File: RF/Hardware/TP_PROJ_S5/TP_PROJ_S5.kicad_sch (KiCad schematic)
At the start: 28 parts, among them J1 Connecteur STLINK V3, J2 DIN-5, J3 Batterie, SW1 Reset Btn, U1 STM32WB55CEUx, U2 BU33SD5WG-TR, Y1 32k, Y2 32 MHZ

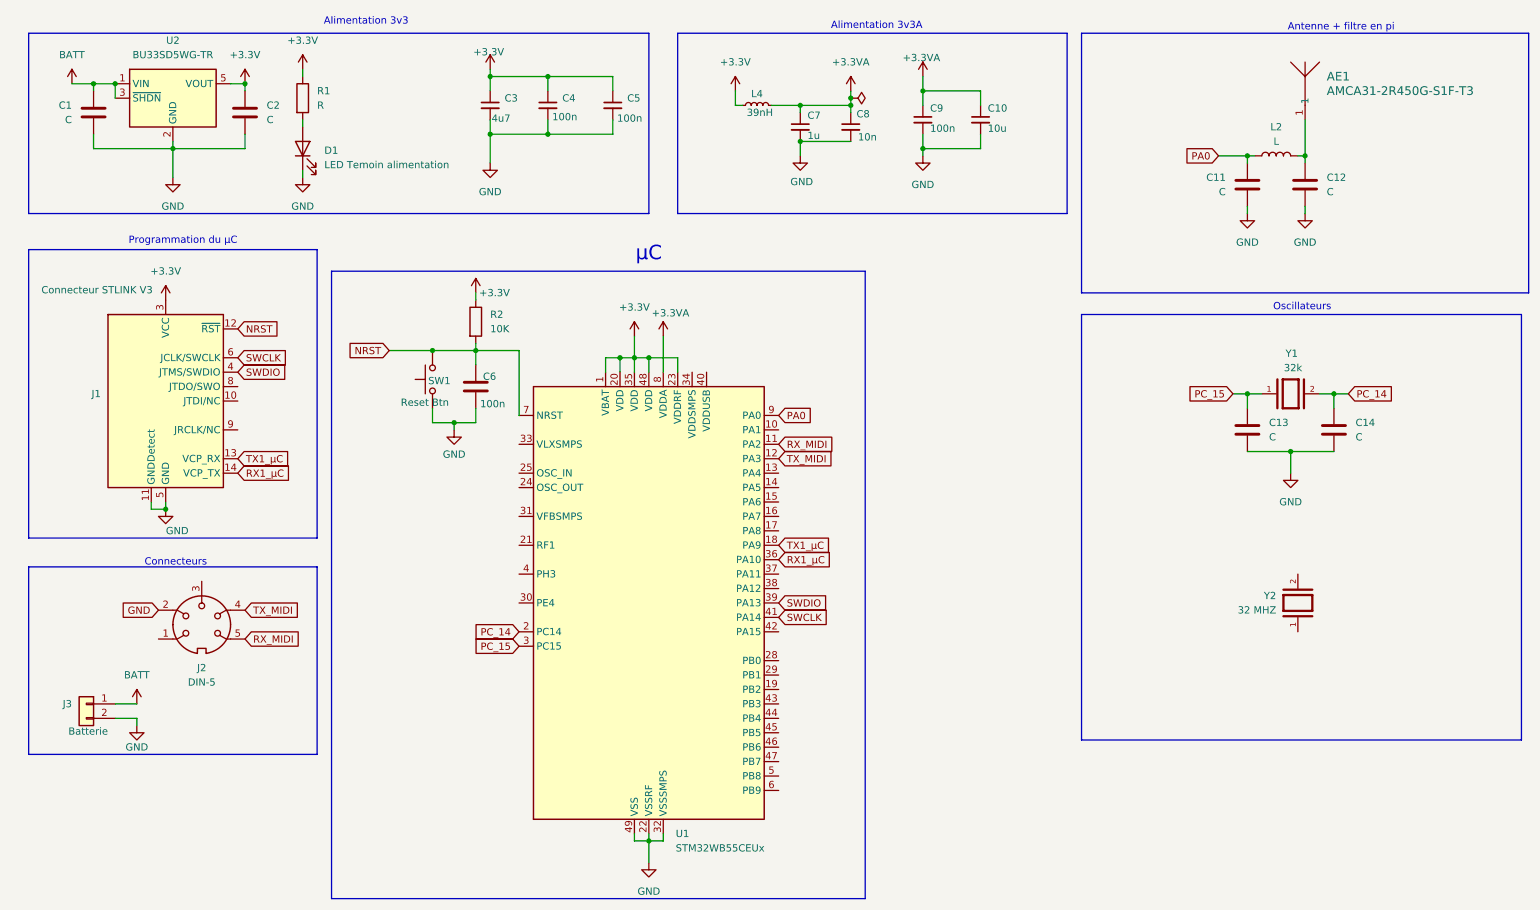
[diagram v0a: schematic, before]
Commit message: Schéma à priori fini, à revoir avec le prof
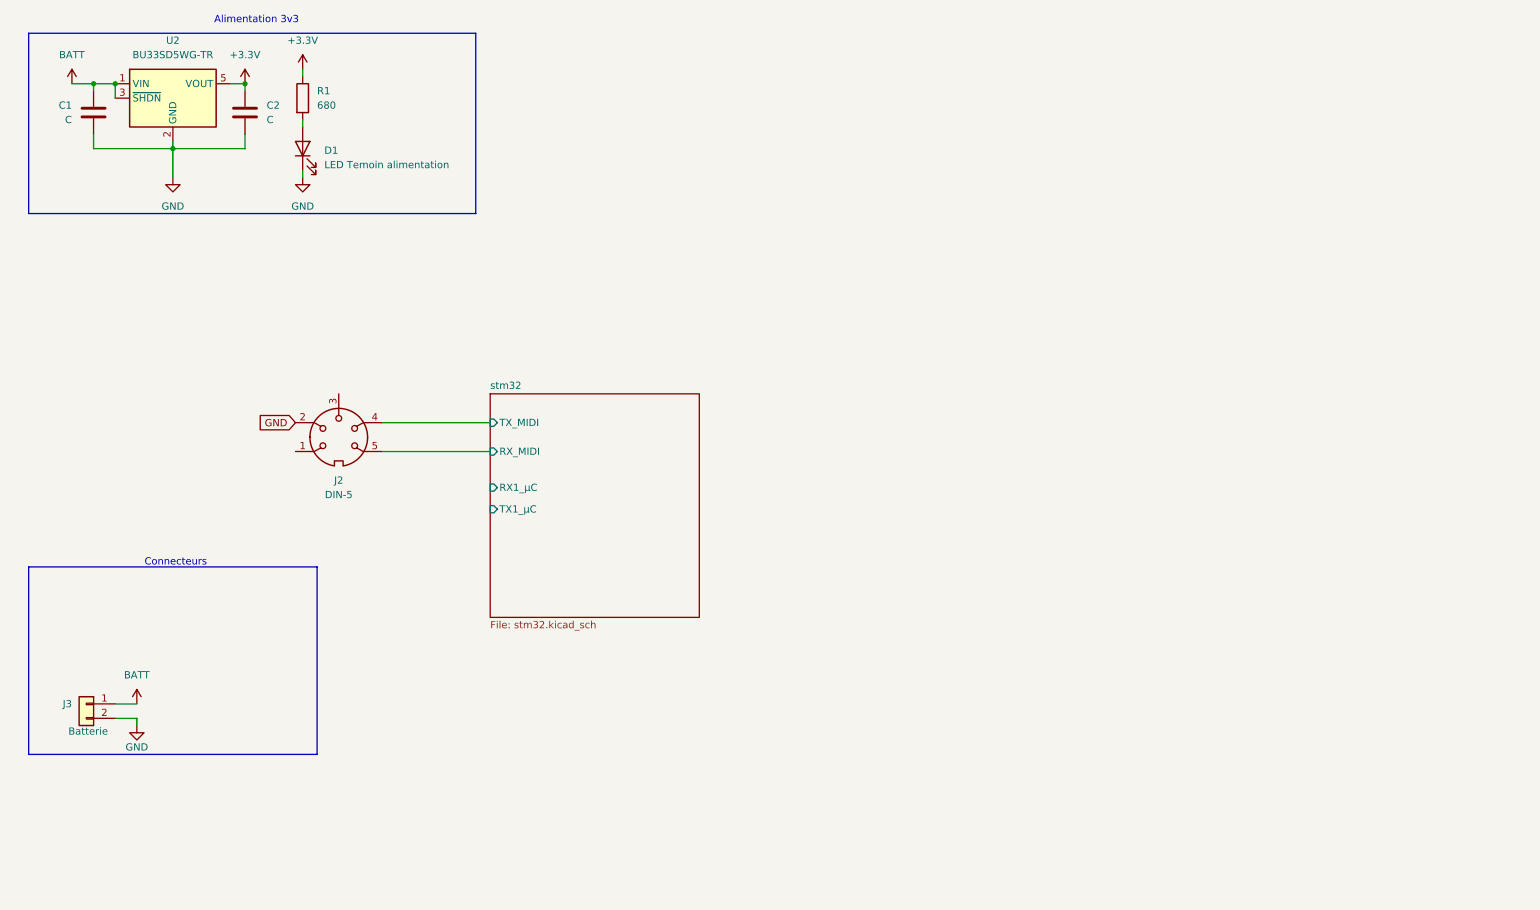
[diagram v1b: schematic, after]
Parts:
- removed AE1: AMCA31-2R450G-S1F-T3, ANT_AMCA31-2R450G-S1F-T3_ABR, symbol 2025-03-03_13-43-06:AMCA31-2R450G-S1F-T3
- removed C10: 10u, Capacitor_SMD:C_0603_1608Metric_Pad1.08x0.95mm_HandSolder, symbol Device:C_Small
- removed C11, C12, C13, C14: C, symbol Device:C
- removed C3: 4u7, Capacitor_SMD:C_0603_1608Metric_Pad1.08x0.95mm_HandSolder, symbol Device:C_Small
- removed C4, C5, C9: 100n, Capacitor_SMD:C_0603_1608Metric_Pad1.08x0.95mm_HandSolder, symbol Device:C_Small
- removed C6: 100n, symbol Device:C
- removed C7: 1u, Capacitor_SMD:C_0603_1608Metric_Pad1.08x0.95mm_HandSolder, symbol Device:C_Small
- removed C8: 10n, Capacitor_SMD:C_0603_1608Metric_Pad1.08x0.95mm_HandSolder, symbol Device:C_Small
- removed J1: Connecteur STLINK V3, Connector_PinHeader_1.27mm:PinHeader_2x07_P1.27mm_Vertical_SMD, symbol Connector:Conn_ST_STDC14
- removed L2: L, symbol Device:L
- removed L4: 39nH, Inductor_SMD:L_0805_2012Metric_Pad1.05x1.20mm_HandSolder, symbol Device:L_Small
- removed R2: 10K, symbol Device:R
- removed SW1: Reset Btn, symbol Switch:SW_Push
- removed U1: STM32WB55CEUx, Package_DFN_QFN:QFN-48-1EP_7x7mm_P0.5mm_EP5.6x5.6mm, symbol MCU_ST_STM32WB:STM32WB55CEUx
- removed Y1: 32k, ABS07AIG32.768KHZ6DT:XTAL_ABS07AIG32.768KHZ6DT, symbol ABS07AIG32.768KHZ6DT:ABS07AIG32.768KHZ6DT
- removed Y2: 32 MHZ, ABS07AIG32.768KHZ6DT:XTAL_ABS07AIG32.768KHZ6DT, symbol ABS07AIG32.768KHZ6DT:ABS07AIG32.768KHZ6DT
- R1: value R -> 680
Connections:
- net RX_MIDI renamed stm32/RX_MIDI
- net TX_MIDI renamed stm32/TX_MIDI
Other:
- added sheet stm32 (stm32.kicad_sch)
- note removed: "Alimentation 3v3A"
- note removed: "Antenne + filtre en pi"
- note removed: "Oscillateurs"
- note removed: "Programmation du µC"
- note removed: "µC"
- moved on the sheet: J2
